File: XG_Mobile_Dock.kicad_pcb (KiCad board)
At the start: 4 copper layers, 158.6 x 80.5 mm, 255 parts, among them J1 5-1775443-8, J16 19V 5A DC, J17 8730, J2 20455-040E-76, J3 20455-040E-76, J4 3-2362375-4, J5 USB_C_Receptacle, J6 USB_C_Receptacle, J7 Conn_02x10_Odd_Even, J8 Conn_02x10_Odd_Even, J9 Conn_01x05, Q1 AON7403, Q2 AON7403, Q3 AON7403, Q4 AON7403, SW1 SW_Push, U1 LM3489QMM/NOPB, U10 SN75LVPE4410RNQR, U11 LM3489QMM/NOPB, U2 TPS65987DDHRSHR, U3 MX25L8006EM1I-12G, U4 VL822-QFN76, U5 AP7331-10WG-7, U6 LM3489QMM/NOPB, U7 TPS2003CDRCR, U8 LM3489QMM/NOPB, U9 SN75LVPE4410RNQR, Y1 25MHz

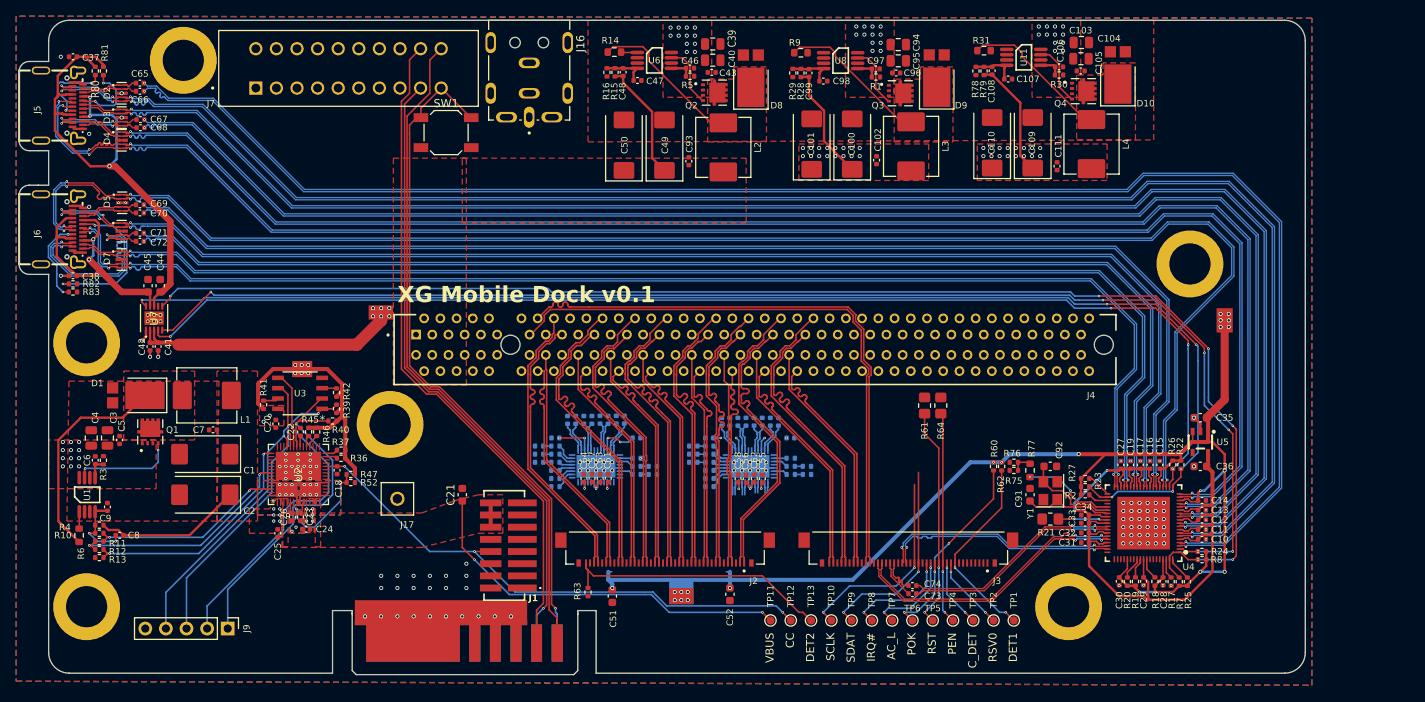
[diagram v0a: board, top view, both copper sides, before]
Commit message: Added MCU
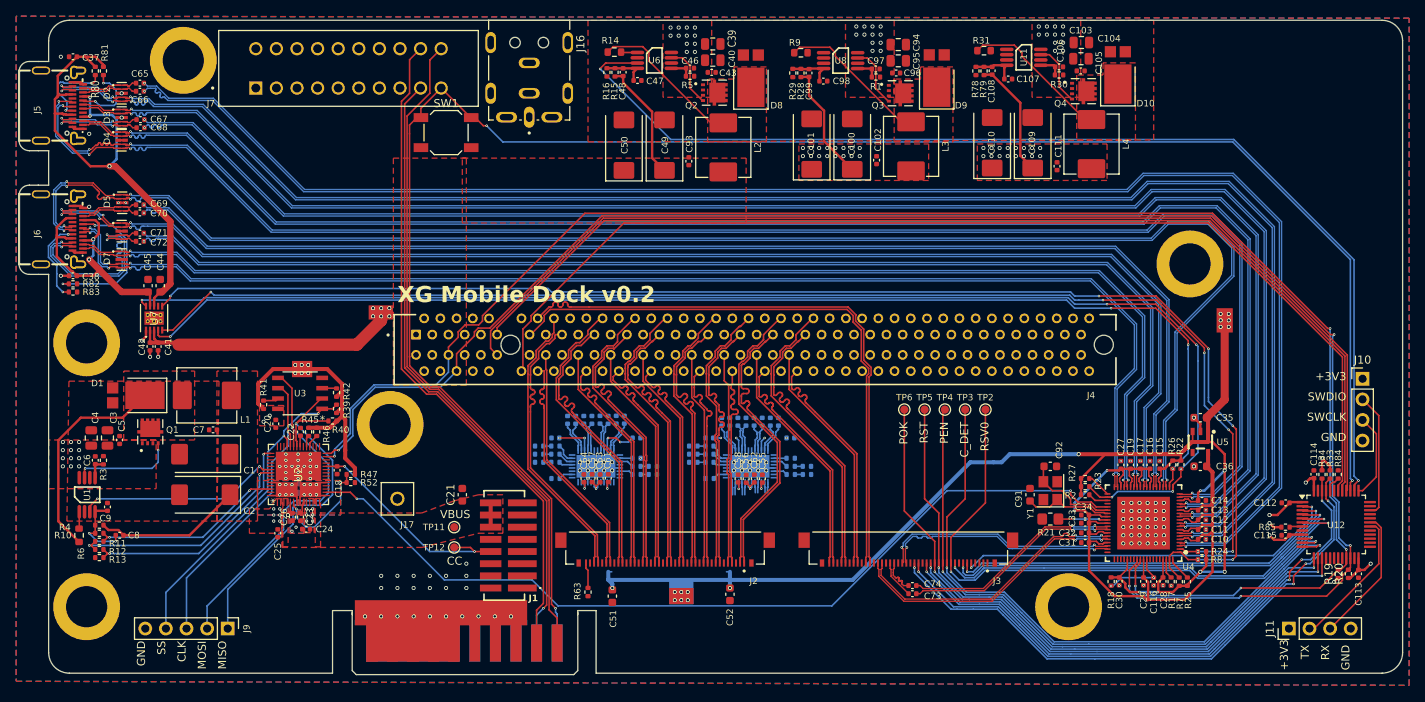
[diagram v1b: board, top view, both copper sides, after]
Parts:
- removed R36, R37, R58, R59, R75: 4.7k, Resistor_SMD:R_0402_1005Metric
- removed R60, R62, R76: 10k, Resistor_SMD:R_0402_1005Metric
- removed R61, R64: 0, Resistor_SMD:R_0805_2012Metric_Pad1.20x1.40mm_HandSolder
- removed R77: 2M, Resistor_SMD:R_0603_1608Metric
- removed TP1, TP10, TP13, TP7, TP8, TP9: TestPoint_Small, TestPoint:TestPoint_Pad_D1.0mm
- added C112: 0.1µF, Capacitor_SMD:C_0402_1005Metric, F.Cu at (152.5, 59.5)
- added C113: 0.1µF, Capacitor_SMD:C_0402_1005Metric, F.Cu at (161.5, 68.2)
- added C114: 0.1µF, Capacitor_SMD:C_0402_1005Metric, F.Cu at (156.0, 56.0)
- added C115: 10µF, Capacitor_SMD:C_0402_1005Metric, F.Cu at (152.5, 63.5)
- added C116: 1µF, Capacitor_SMD:C_0402_1005Metric, F.Cu at (136.2, 69.2)
- added J10: SWD, Connector_PinHeader_2.54mm:PinHeader_1x04_P2.54mm_Vertical, F.Cu at (162.0, 44.2)
- added J11: UART, Connector_PinHeader_2.54mm:PinHeader_1x04_P2.54mm_Vertical, F.Cu at (152.9, 75.0)
- added R84: 1k, Resistor_SMD:R_0402_1005Metric, F.Cu at (159.0, 56.0)
- added R85: 10k, Resistor_SMD:R_0402_1005Metric, F.Cu at (152.5, 62.5)
- added U12: STM32F030C8Tx, Package_QFP:LQFP-48_7x7mm_P0.5mm, F.Cu at (158.8, 62.2)
- R33, R34: value 4.7k -> 10k; moved to F.Cu
- moved R33 95.5 mm to (158.0, 56.0), turned to -90 degrees
- moved R34 94.5 mm to (157.0, 56.0), turned to -90 degrees
- moved TP12 42.5 mm to (50.0, 65.0), turned to 90 degrees
- moved TP11 40.7 mm to (50.0, 62.5), turned to 90 degrees
- moved R20 27.3 mm to (160.2, 68.2)
- moved TP2 26.0 mm to (115.5, 48.0)
- moved TP3 26.0 mm to (113.0, 48.0)
- moved TP4 26.0 mm to (110.5, 48.0)
- moved TP5 26.0 mm to (108.0, 48.0)
- moved TP6 26.0 mm to (105.5, 48.0)
- moved R19 25.0 mm to (159.0, 68.3)
- moved R18 5.40 mm to (131.0, 69.2), turned to 90 degrees
- moved R35 1.00 mm to (62.5, 56.5)
- moved R51 1.00 mm to (81.5, 56.5)
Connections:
- net /DET2 renamed /DET
- net /PWREN renamed /PWREN#
- net /RST renamed /RST#
- net Net-(J3-CON_DET) renamed /CON_DET
- net Net-(J3-Pad10) renamed /RSV0
- J3 pad 1: unconnected-(J3-Pad1) -> +3V3
- J3 pad 15: Net-(J3-P_AC_LOSS) -> /AC_LOSS
- J3 pad 16: Net-(J3-MCU_IRQ#) -> /MCU_IRQ#
- J3 pad 18: /SMDAT -> /SDA1
- J3 pad 19: /SMCLK -> /SCL1
- J3 pad 2: unconnected-(J3-Pad2) -> +3V3
- J3 pad 3: unconnected-(J3-Pad3) -> +3V3
- J3 pad 4: unconnected-(J3-Pad4) -> +3V3
- J3 pad 5: unconnected-(J3-Pad5) -> /LOCK_SW
- J3 pad 6: unconnected-(J3-Pad6) -> /LED_WHITE#
- J3 pad 7: unconnected-(J3-Pad7) -> /LED_RED#
- J3 pad 9: /DET1 -> /LOCK_DET
- J4 pad A11: /PERST -> /PERST#
- J4 pad B11: unconnected-(J4-PadB11) -> /WAKE#
- J4 pad B12: /CLKREQ -> /CLKREQ#
- J4 pad B5: /SMCLK -> /SCL2
- J4 pad B6: /SMDAT -> /SDA2
- R19 pad 2: /USB Hub/SMCLK -> /SCL2
- R20 pad 2: /USB Hub/SMDAT -> /SDA2
- R33 pad 1: Net-(U9-SDA) -> +3V3
- R33 pad 2: +3V3 -> /SCL1
- R34 pad 1: Net-(U9-SCL) -> +3V3
- R34 pad 2: +3V3 -> /SDA1
- U1 pad 3: unconnected-(U1-EN-Pad3) -> /USB PD Charger/POWER_EN
- U10 pad 3: Net-(U10-SCL) -> /PCIe Redriver/SCL
- U10 pad 4: Net-(U10-SDA) -> /PCIe Redriver/SDA
- U2 pad 27: Net-(U2-I2C1_SCL) -> /SCL2
- U2 pad 28: Net-(U2-I2C1_SDA) -> /SDA2
- U2 pad 48: unconnected-(U2-GPIO16-Pad48) -> /USB PD Charger/POWER_EN
- U4 pad 65: /USB Hub/SMDAT -> /SDA2
- U4 pad 66: /USB Hub/SMCLK -> /SCL2
- U6 pad 3: unconnected-(U6-EN-Pad3) -> /12V_EN
- U9 pad 3: Net-(U9-SCL) -> /PCIe Redriver/SCL
- U9 pad 4: Net-(U9-SDA) -> /PCIe Redriver/SDA
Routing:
- net /SDA2: track 0.00 -> 209.7 mm, vias 0 -> 5
- net /SCL2: track 0.00 -> 209.2 mm, vias 0 -> 5
- net /PWR_SW: track 83.7 -> 228.1 mm, vias 1 -> 3
- net /WAKE#: track 0.00 -> 138.5 mm
- net /12V_EN: track 0.00 -> 136.5 mm, vias 0 -> 2
- net /CLKREQ#: track 0.00 -> 135.9 mm
- net /PERST#: track 0.00 -> 134.9 mm
- net /USB Hub/VBUSDET: track 11.4 -> 109.1 mm
- net /SCL1: track 0.00 -> 72.1 mm, vias 0 -> 4
- net /SDA1: track 0.00 -> 70.8 mm, vias 0 -> 4
- net /CON_DET: track 8.43 -> 76.1 mm
- net /RSV0: track 9.25 -> 75.6 mm
- net /MCU_IRQ#: track 0.00 -> 60.2 mm, vias 0 -> 2
- net /AC_LOSS: track 0.00 -> 58.7 mm, vias 0 -> 2
- net /LOCK_DET: track 0.00 -> 53.3 mm, vias 0 -> 2
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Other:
- board size 158.6 x 80.5 mm -> 170.6 x 80.5 mm
- board text added: "+3V3"
- board text added: "CLK"
- board text added: "GND"
- board text added: "MISO"
- board text added: "MOSI"
- board text added: "RX"
- board text added: "SS"
- board text added: "SWCLK"
- board text added: "SWDIO"
- board text added: "TX"
- board text added: "XG Mobile Dock v0.2"
- board text removed: "AC_L"
- board text removed: "DET1"
- board text removed: "DET2"
- board text removed: "IRQ#"
- board text removed: "SCLK"
- board text removed: "SDAT"
- board text removed: "XG Mobile Dock v0.1"
